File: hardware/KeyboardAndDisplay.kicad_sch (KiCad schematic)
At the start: 34 parts, among them SW301 Q/1/STOP, SW302 W/2/CH0, SW303 E/3/CH1, SW304 R/4/CH2, SW305 T/5/CH3, SW306 Y/6/_, SW307 U/7/-, SW308 I/8/+, SW309 O/9/=, SW310 P/0, SW311 A/!/`, SW312 S/"/CH4, SW313 D/$/CH5, SW314 F/%/CH6, SW315 G/^/CH7, SW316 H/&/{, SW317 J/*/}, SW318 K/(/[, SW319 L/)/], SW320 BKSP/DEL, SW321 SHIFT, SW322 Z/\/|, SW323 X/;/:, SW324 C/'/@, SW325 V/#/~, SW326 B/,/<, SW327 N/./>, SW328 M///?, SW329 SYM, SW330 SPC/ENT, U301 MCP23S17_SP, U302 NHD-0420DZ-FL-YBW

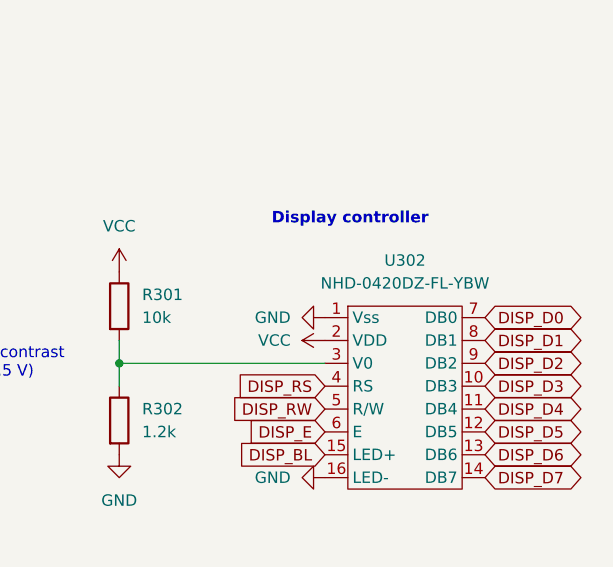
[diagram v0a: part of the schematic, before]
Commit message: Modify power circuitry to use better diode arrangement and more energy-efficient regulator
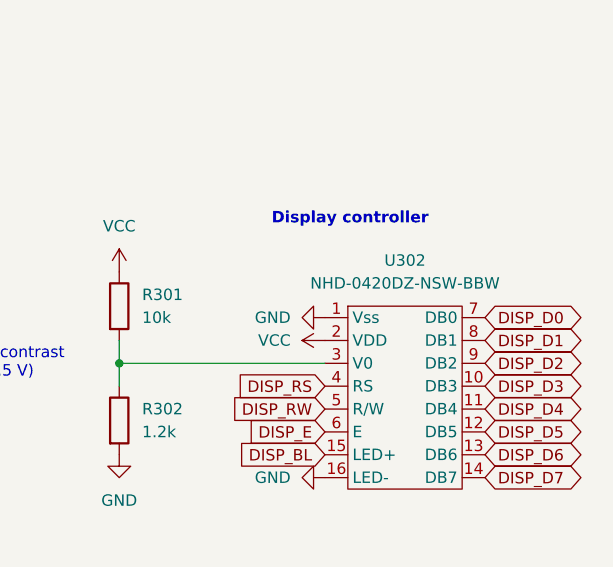
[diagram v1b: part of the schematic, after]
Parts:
- U302: value NHD-0420DZ-FL-YBW -> NHD-0420DZ-NSW-BBW
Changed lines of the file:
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@@
 			)
 		)
-		(property "Value" "NHD-0420DZ-FL-YBW"
+		(property "Value" "NHD-0420DZ-NSW-BBW"
 			(at 234.95 86.36 0)
 			(effects
